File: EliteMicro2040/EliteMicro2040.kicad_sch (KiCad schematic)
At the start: 41 parts, among them J2 B3U, J5 Conn_01x03_Male, U1 SPX3819M5-L-3-3, U2 Elite-C, U3 RP2040, U4 W25Q32JVSS, Y1 3225_4P

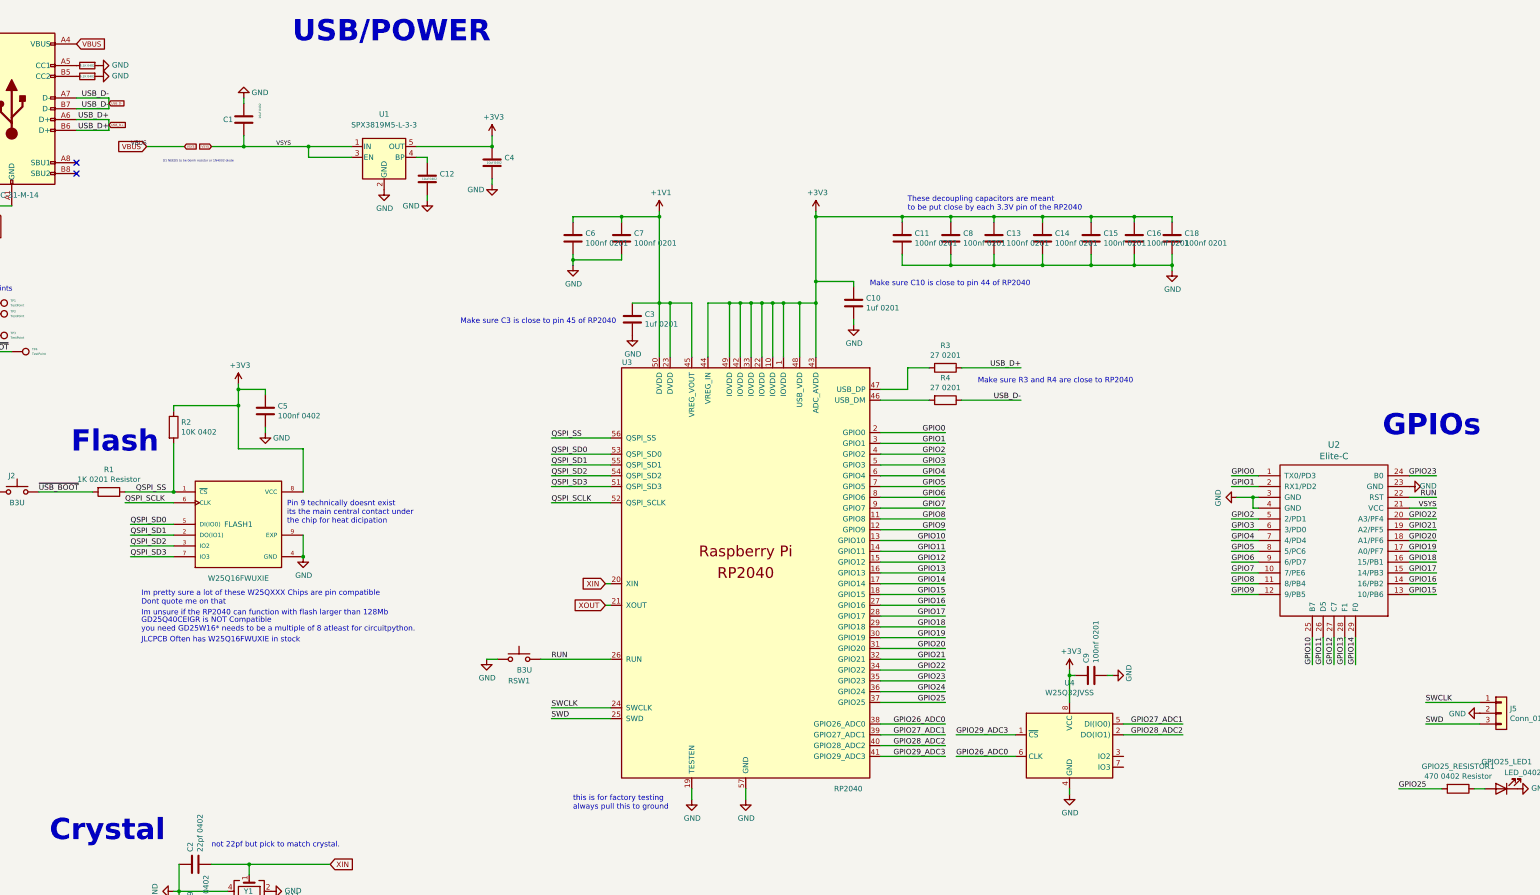
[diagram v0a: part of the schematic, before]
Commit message: matched pinout of pro-micro a bit more among various other changes.
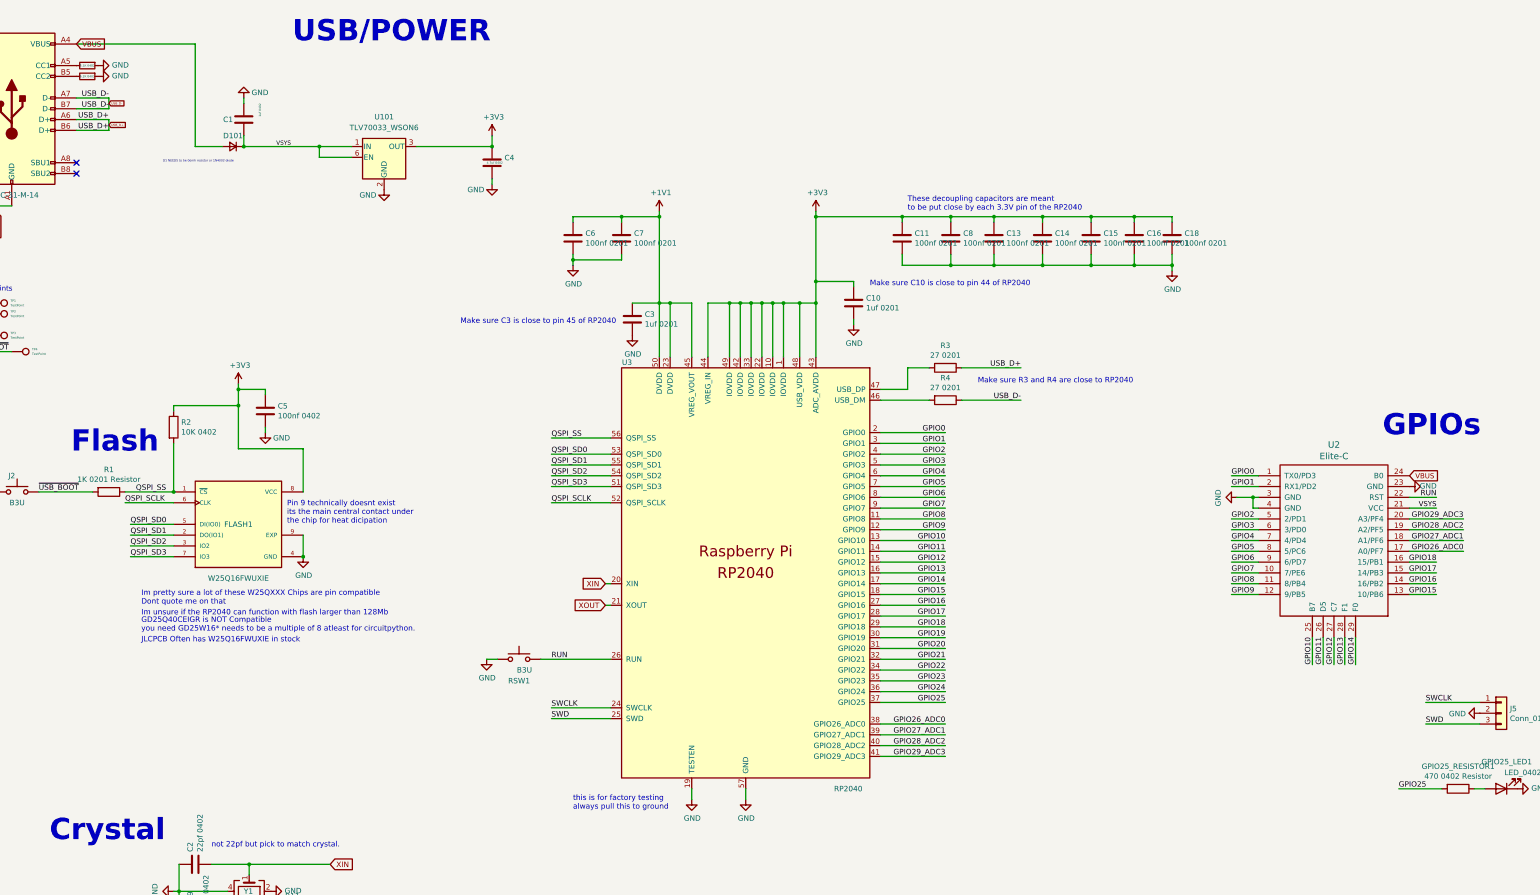
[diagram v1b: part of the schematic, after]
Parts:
- removed C12: 10uf 0402, Capacitor_SMD:C_0402_1005Metric, symbol Device:C
- removed C9: 100nf 0201, Capacitor_SMD:C_0201_0603Metric, symbol Device:C
- removed U1: SPX3819M5-L-3-3, Package_TO_SOT_SMD:SOT-23-5, symbol Regulator_Linear:SPX3819M5-L-3-3
- removed U4: W25Q32JVSS, Package_SON:SON-8-1EP_3x2mm_P0.5mm_EP1.4x1.6mm, symbol Memory_Flash:W25Q32JVSS
- added D101: 1n4002, Diode_SMD:D_SOD-523, symbol Device:D_Small
- added U101: TLV70033_WSON6, Package_SON:WSON-6_1.5x1.5mm_P0.5mm, symbol Regulator_Linear:TLV70033_WSON6
- C1: value 10uf 0402 -> 1uf 0402
- C10, C11, C13, C14, C15, C16, C18, C3, C6, C7, C8, R1, R11: footprint Capacitor_SMD:C_0201_0603Metric -> Capacitor_SMD:C_0402_1005Metric
- C4: value 10uf 0402 -> 4.7uf 0402
- R3, R4: footprint Resistor_SMD:R_0201_0603Metric -> Resistor_SMD:R_0402_1005Metric
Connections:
- net +3V3: now also U101.3 (OUT)
- net GND: now also U101.2 (GND)
- net GPIO19: no longer U2.17 (A0/PF7)
- net GPIO20: no longer U2.18 (A1/PF6)
- net GPIO21: no longer U2.19 (A2/PF5)
- net GPIO22: no longer U2.20 (A3/PF4)
- net GPIO23: no longer U2.24 (B0)
- net GPIO26_ADC0: now also U2.17 (A0/PF7)
- net GPIO27_ADC1: now also U2.18 (A1/PF6)
- net GPIO28_ADC2: now also U2.19 (A2/PF5)
- net GPIO29_ADC3: now also U2.20 (A3/PF4)
- net VBUS: now also U2.24 (B0), D101.2 (A); no longer C1.1, U2.21 (VCC)
- new net VSYS: C1.1, D101.1 (K), U101.1 (IN), U101.6 (EN), U2.21 (VCC)

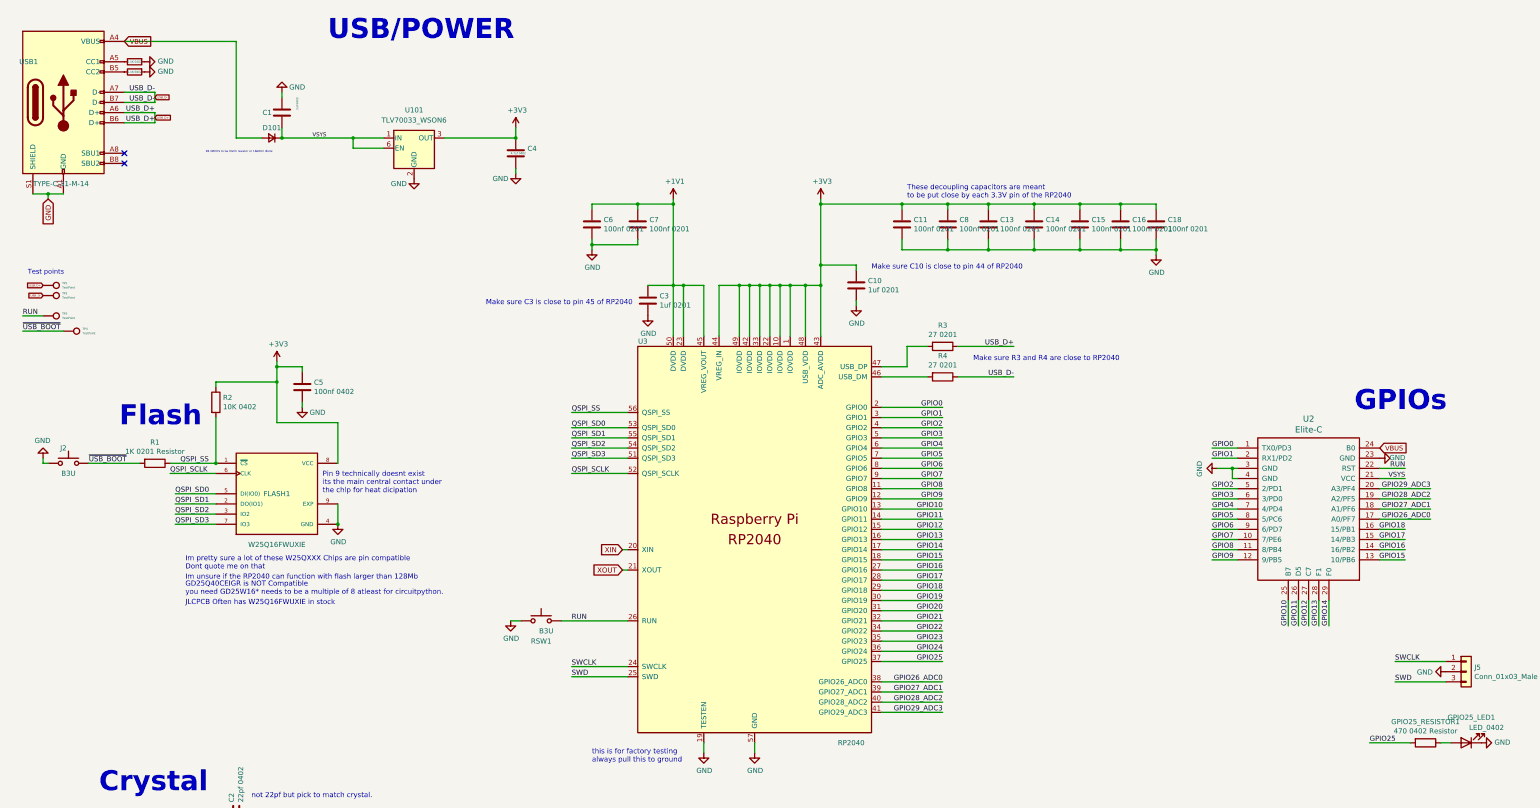
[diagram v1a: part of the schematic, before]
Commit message: modified board to fit with bastardKB's standard, added vbus sense, changed pinout, removed reset button and moved bootsel, removed SPI EEPROM as its not supported.
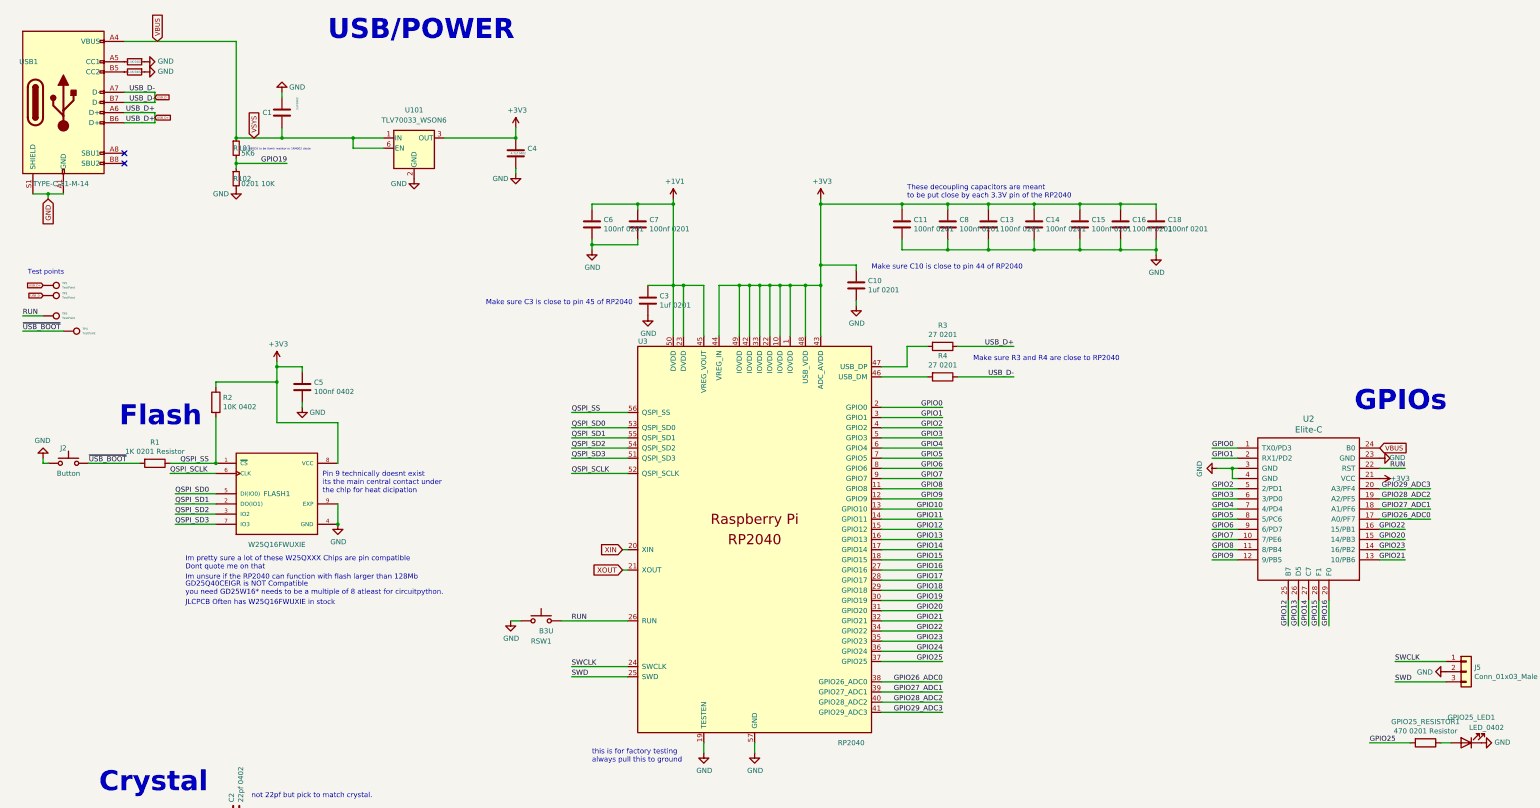
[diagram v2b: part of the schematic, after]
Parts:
- removed D101: 1n4002, Diode_SMD:D_SOD-523, symbol Device:D_Small
- added R101: 5K6, Diode_SMD:D_0402_1005Metric, symbol Device:R_Small
- added R102: 0201 10K, Diode_SMD:D_0201_0603Metric, symbol Device:R_Small
- GPIO25_RESISTOR1: value 470 0402 Resistor -> 470 0201 Resistor; footprint Resistor_SMD:R_0402_1005Metric -> Resistor_SMD:R_0201_0603Metric
- J2: value B3U -> Button; footprint Button_Switch_SMD:SW_SPST_B3U-1000P -> Button_Switch_SMD:SW_SPST_CK_KXT3
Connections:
- net +3V3: now also U2.21 (VCC)
- net GND: now also R102.2
- net GPIO10: no longer U2.25 (B7)
- net GPIO11: no longer U2.26 (D5)
- net GPIO12: now also U2.25 (B7); no longer U2.27 (C7)
- net GPIO13: now also U2.26 (D5); no longer U2.28 (F1)
- net GPIO14: now also U2.27 (C7); no longer U2.29 (F0)
- net GPIO15: now also U2.28 (F1); no longer U2.13 (10/PB6)
- net GPIO16: now also U2.29 (F0); no longer U2.14 (16/PB2)
- net GPIO17: no longer U2.15 (14/PB3)
- net GPIO18: no longer U2.16 (15/PB1)
- net GPIO19: now also R101.2, R102.1
- net GPIO20: now also U2.15 (14/PB3)
- net GPIO21: now also U2.13 (10/PB6)
- net GPIO22: now also U2.16 (15/PB1)
- net GPIO23: now also U2.14 (16/PB2)
- net VBUS: now also C1.1, U101.1 (IN), U101.6 (EN), R101.1
- removed net VSYS: C1.1, U101.1 (IN), U101.6 (EN), U2.21 (VCC)

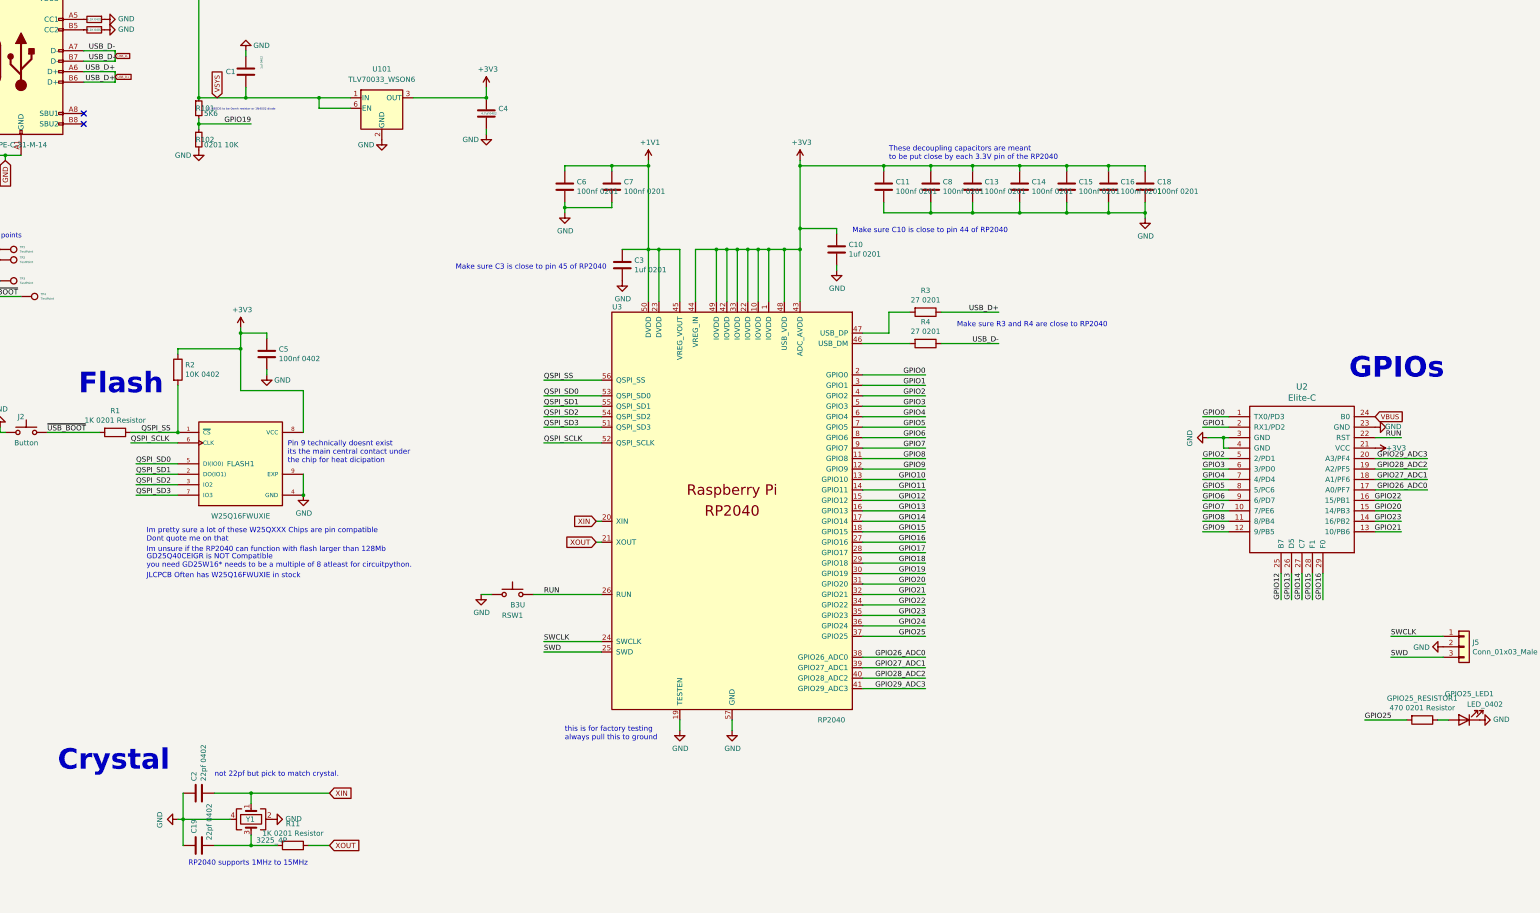
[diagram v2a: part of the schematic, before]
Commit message: lots of changes, swapped many parts to 0402, swapped SOT regulator to small WSON, made sure there is proper parity between footprint and value, etc etc etc
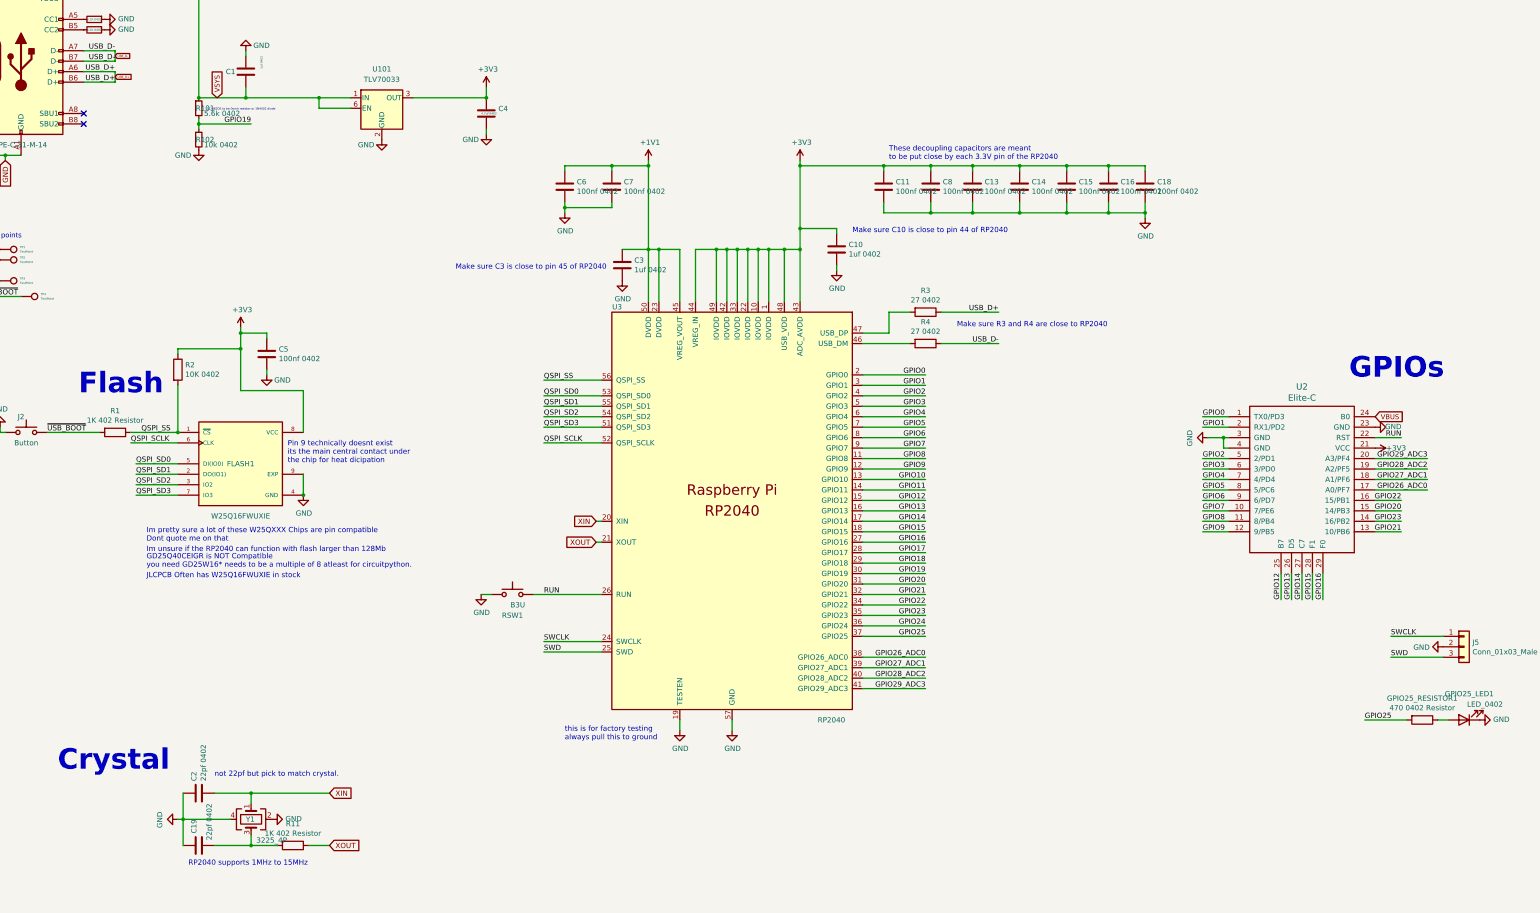
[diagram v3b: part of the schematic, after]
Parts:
- C10, C3: value 1uf 0201 -> 1uf 0402
- C11, C13, C14, C15, C16, C18, C6, C7, C8: value 100nf 0201 -> 100nf 0402
- GPIO25_RESISTOR1: value 470 0201 Resistor -> 470 0402 Resistor; footprint Resistor_SMD:R_0201_0603Metric -> Resistor_SMD:R_0402_1005Metric
- R1, R11: value 1K 0201 Resistor -> 1K 402 Resistor
- R101: value 5K6 -> 5.6k 0402; footprint Diode_SMD:D_0402_1005Metric -> Resistor_SMD:R_0402_1005Metric
- R102: value 0201 10K -> 10k 0402; footprint Diode_SMD:D_0201_0603Metric -> Resistor_SMD:R_0402_1005Metric
- R3, R4: value 27 0201 -> 27 0402
- U101: value TLV70033_WSON6 -> TLV70033

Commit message: made some smaller components generated new gerber
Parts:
- Y1: value 3225_4P -> 2520_4P 12Mhz; footprint Crystal:Crystal_SMD_3225-4Pin_3.2x2.5mm -> Crystal:Crystal_SMD_2520-4Pin_2.5x2.0mm
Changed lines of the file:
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@@
     (effects (font (size 1.27 1.27)) (justify left bottom))
   )
-  (text "RP2040 supports 1MHz to 15MHz" (at 66.04 231.14 0)
+  (text "RP2040 supports 1MHz to 15MHz" (at 66.04 232.41 0)
     (effects (font (size 1.27 1.27)) (justify left bottom))
   )
@@
       (effects (font (size 1.27 1.27)) (justify left))
     )
-    (property "Value" "3225_4P" (id 1) (at 82.55 224.79 90)
-      (effects (font (size 1.27 1.27)) (justify left))
-    )
-    (property "Footprint" "Crystal:Crystal_SMD_3225-4Pin_3.2x2.5mm" (id 2) (at 81.28 219.71 0)
+    (property "Value" "2520_4P 12Mhz" (id 1) (at 95.25 220.345 90)
+      (effects (font (size 1.27 1.27)) (justify left))
+    )
+    (property "Footprint" "Crystal:Crystal_SMD_2520-4Pin_2.5x2.0mm" (id 2) (at 81.28 219.71 0)
       (effects (font (size 1.27 1.27)) hide)
     )
@@
   (symbol (lib_id "Device:R") (at 91.44 226.06 270) (unit 1)
     (in_bom yes) (on_board yes)
-    (property "Reference" "R11" (id 0) (at 91.44 220.8022 90))
-    (property "Value" "1K 402 Resistor" (id 1) (at 91.44 223.1136 90))
+    (property "Reference" "R11" (id 0) (at 91.44 226.06 90))
+    (property "Value" "1K 402 Resistor" (id 1) (at 91.44 228.6 90))
     (property "Footprint" "Capacitor_SMD:C_0402_1005Metric" (id 2) (at 91.44 224.282 90)
       (effects (font (size 1.27 1.27)) hide)
@@
     )
     (path "/00000000-0000-0000-0000-0000612055a1"
-      (reference "Y1") (unit 1) (value "3225_4P") (footprint "Crystal:Crystal_SMD_3225-4Pin_3.2x2.5mm")
-    )
-  )
+      (reference "Y1") (unit 1) (value "2520_4P 12Mhz") (footprint "Crystal:Crystal_SMD_2520-4Pin_2.5x2.0mm")
+    )
+  )
